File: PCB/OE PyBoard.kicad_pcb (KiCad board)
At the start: 4 copper layers, 33 x 41.9 mm, 57 parts, among them J1 Conn_01x08, J10 USB4105-GF-A, J8 Conn_02x03_Odd_Even, J9 Conn_01x08, U1 STM32F405RGT6, U2 MCP1700T, X1 12 MHz, X2 32.768 kHz

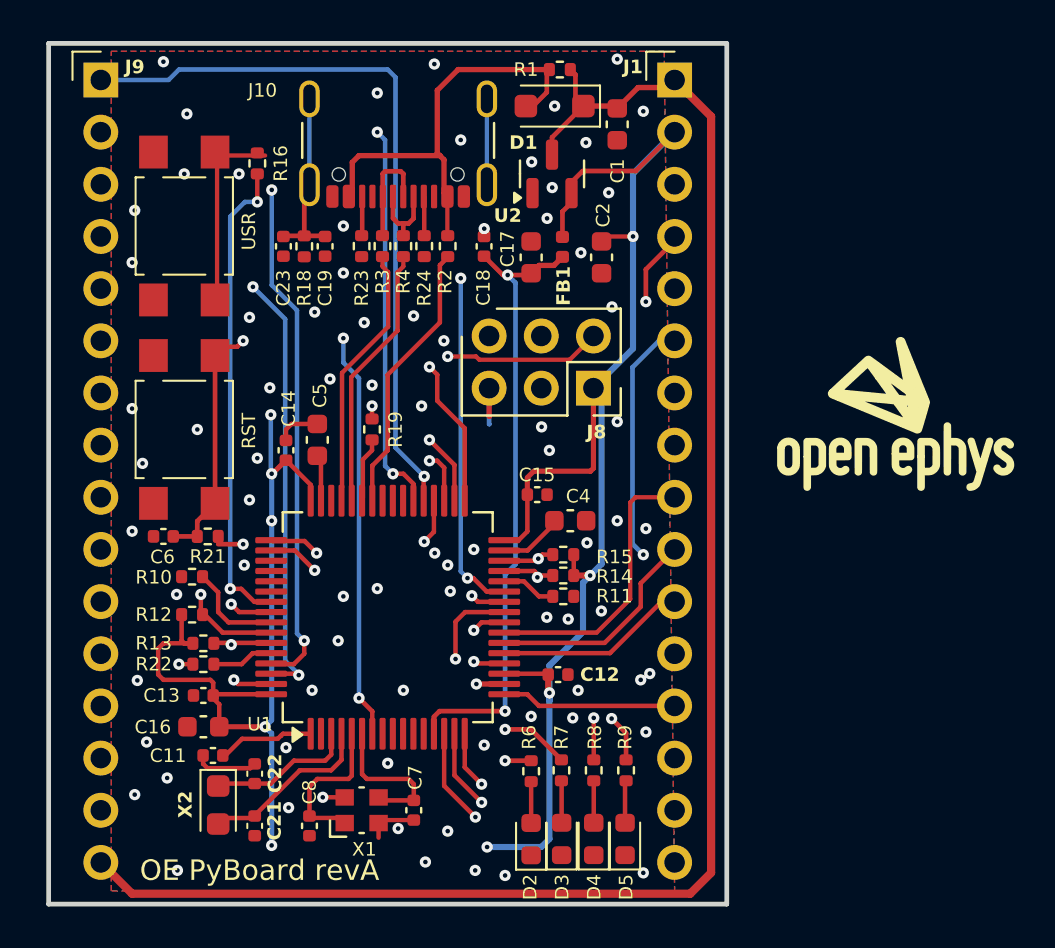
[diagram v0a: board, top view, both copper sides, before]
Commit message: OE-PyBoard - revisão depois de avaliação Filipe
- nome do projecto/ficheiros alterados para OE-PyBoard
- Colocar OEPS logo para o bottom, e colocar no meio da board
- X1: Mudar a referência para a parte de cima
- udar o diode D1 para 2A & aumentar a secção das linhas VBUS
- alterado o sinal VIN para V+, para ficar coerente com a board original
- passar X2 & C21 & C22 para assembled
- R1=0R passada a solder-jumper
- acrescentadas Labels nos pinos laterais

- gerados production-files
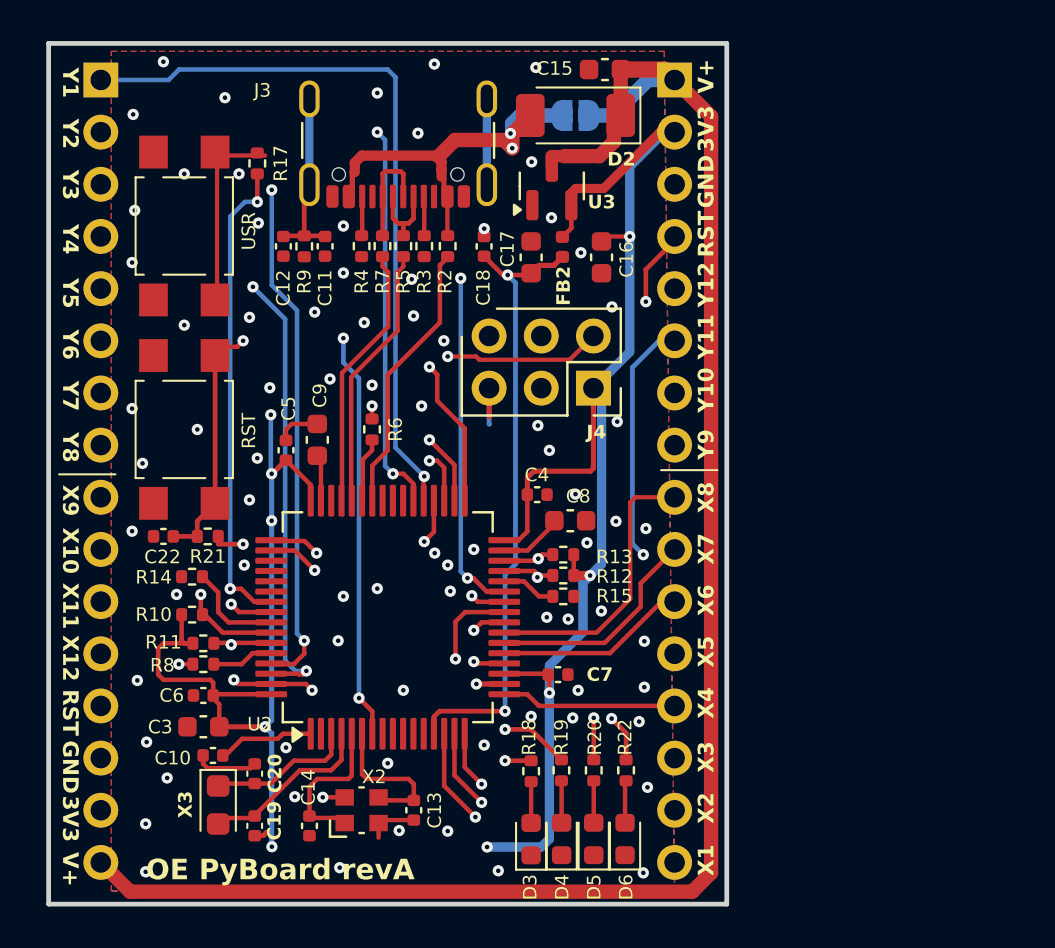
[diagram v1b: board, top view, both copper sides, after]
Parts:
- removed G***: LOGO, FED3_PCBLib:oe logo
- added REF**: OEPS Logo, OE PyBoard FootprintLib:OEPS Logo, B.Cu at (142.2, 115.3)
- C10: renamed from C11; value 100n -> 100nF
- C15: renamed from C1; value 2u2 -> 2.2uF
- C16: renamed from C2; value 4u7 -> 4.7uF
- C17: value 4.7u -> 4.7uF
- C18: value 100n -> 100nF
- C22: renamed from C6; value 100n -> 100nF
- C3: renamed from C16; value 4.7u -> 4.7uF
- C4: renamed from C15; value 100n -> 100nF
- C5: renamed from C14; value 100n -> 100nF
- C6: renamed from C13; value 100n -> 100nF
- C7: renamed from C12; value 100n -> 100nF
- C8: renamed from C4; value 2u2 -> 2.2uF
- C9: renamed from C5; value 2u2 -> 2.2uF
- D2: renamed from D1; footprint Diode_SMD:D_SOD-123F -> Diode_SMD:D_SOD-128
- JP2: renamed from R1; footprint Resistor_SMD:R_0402_1005Metric -> Jumper:SolderJumper-2_P1.3mm_Open_RoundedPad1.0x1.5mm; moved to B.Cu
- moved C15 2.73 mm to (152.8, 95.5), turned to 180 degrees
- moved JP2 2.36 mm to (151.4, 97.7)
- moved D2 1.11 mm to (151.4, 97.7)
- moved U3 0.59 mm to (150.2, 101.2)
- renumbered C19 to C11, C23 to C12, C7 to C13, C8 to C14, C21 to C19, C22 to C20, D2 to D3, D3 to D4, D4 to D5, D5 to D6, FB1 to FB2, J10 to J3, J8 to J4, J9 to J6, J1 to J7, R12 to R10, R13 to R11, R14 to R12, R15 to R13, R10 to R14, R11 to R15, R16 to R17, R6 to R18, R7 to R19, R8 to R20, R9 to R22, R24 to R3, R23 to R4, R4 to R5, R19 to R6, R3 to R7, R22 to R8, R18 to R9, RST1 to RST2, U1 to U2, U2 to U3, USR1 to USR2, X1 to X2, X2 to X3
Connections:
- net VIN renamed V+
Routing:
- net V+: track 79.4 -> 85.4 mm
- net GND: track 15.7 -> 19.9 mm
- net +3V3: track 133.8 -> 134.9 mm
- net /PB9-Y4: track 29.6 -> 30.3 mm
- net VBUS: track 21.1 -> 20.5 mm, vias 0 -> 2
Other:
- board text added: "3V3"
- board text added: "GND"
- board text added: "V+"
- board text added: "X1"
- board text added: "X10"
- board text added: "X11"
- board text added: "X12"
- board text added: "X2"
- board text added: "X3"
- board text added: "X4"
- board text added: "X5"
- board text added: "X6"
- board text added: "X7"
- board text added: "X8"
- board text added: "X9"
- board text added: "Y1"
- board text added: "Y10"
- board text added: "Y11"
- board text added: "Y12"
- board text added: "Y2"
- board text added: "Y3"
- board text added: "Y4"
- board text added: "Y5"
- board text added: "Y6"
- board text added: "Y7"
- board text added: "Y8"
- board text added: "Y9"

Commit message: modificada refª de origem para P&P
- modificada refª de origem de P&P p/a canto inferior esqº
- gerados novos ficheiros  de P&P
- outros ficheiros Gerbers de produção sem modificações
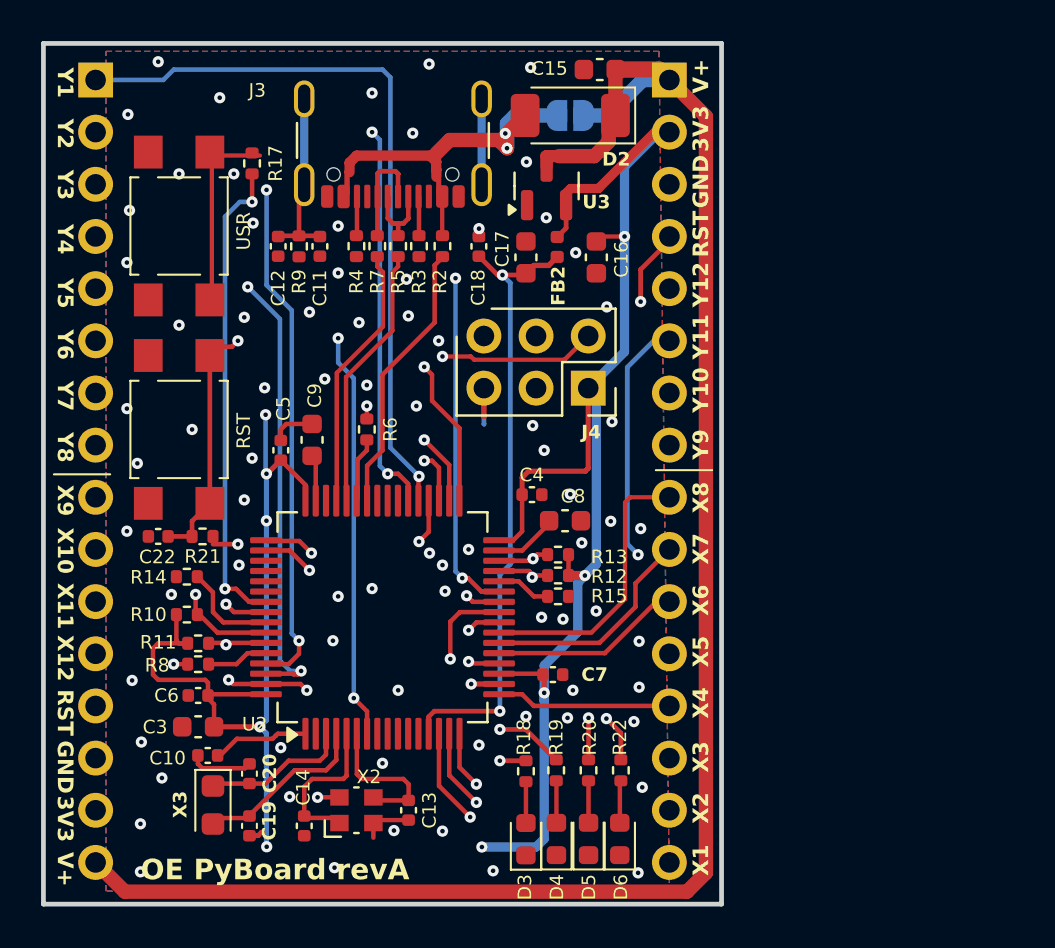
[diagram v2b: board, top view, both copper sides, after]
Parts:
- moved C11 0.25 mm to (138.9, 104.1)
- moved C14 0.25 mm to (138.2, 132.3)
- moved C19 0.25 mm to (135.5, 132.3)
- moved C20 0.25 mm to (135.5, 129.8)
- moved C22 0.25 mm to (131.1, 118.2)
- moved C3 0.25 mm to (133.0, 127.5)
- moved C4 0.25 mm to (149.3, 116.2)
- moved C5 0.25 mm to (137.0, 114.0)
- moved C6 0.25 mm to (133.0, 126.0)
- moved C9 0.25 mm to (138.6, 113.5)
- moved J4 0.25 mm to (152.0, 111.0)
- moved J6 0.25 mm to (128.0, 96.0)
- moved J7 0.25 mm to (156.0, 96.0)
- moved R11 0.25 mm to (133.0, 123.4)
- moved R19 0.25 mm to (150.4, 129.6)
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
